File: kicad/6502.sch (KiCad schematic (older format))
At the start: 8 parts

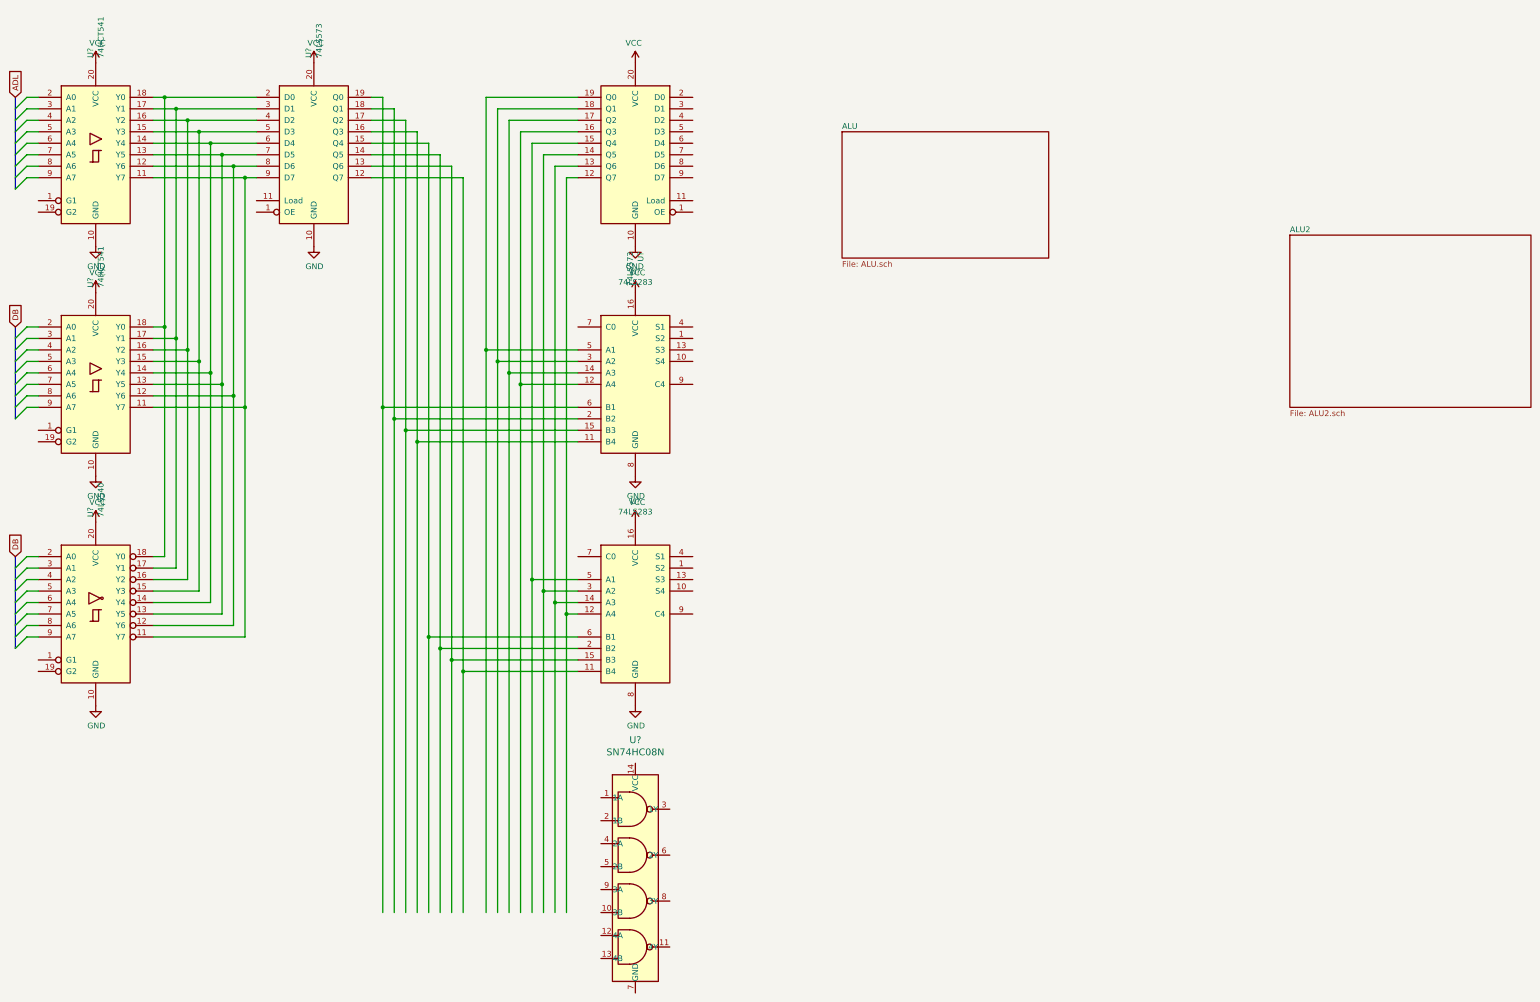
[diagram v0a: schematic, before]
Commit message: add ALU schematic
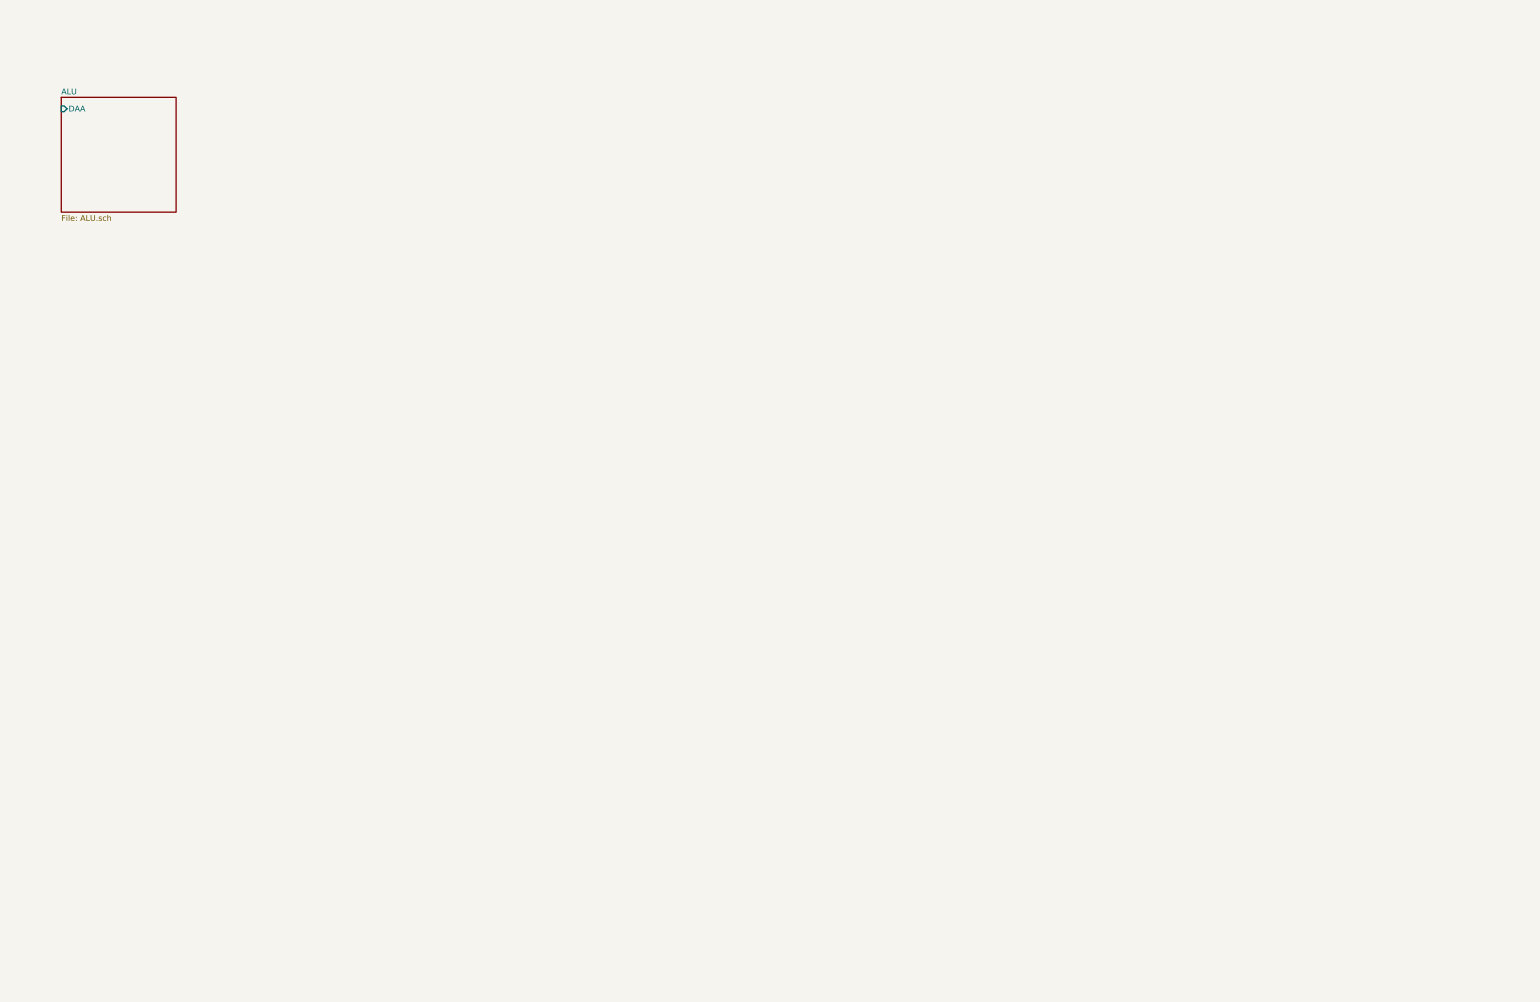
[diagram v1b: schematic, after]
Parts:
- removed U? (x2): 74LS573, symbol 74xx:74LS573
- removed U? (x2): 74HCT541, symbol 74xx:74HCT541
- removed U?: 74LS540, symbol 74xx:74LS540
- removed U? (x2): 74LS283, symbol 74xx:74LS283
- removed U?: SN74HC08N, digikey-footprints:DIP-14_W3mm, symbol dk_Logic-Gates-and-Inverters:SN74HC08N
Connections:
- net labels removed: ADL, DB, GND, VCC
- wire segments 136 -> 0

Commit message: ALU progress
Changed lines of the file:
@@
 F1 "ALU.sch" 50
 F2 "DAA" I L 1000 1100 50
+F3 "HC" I L 1000 1200 50
+F4 "1-ADDC" I L 1000 1300 50
+F5 "ACR" O R 2000 1100 50
+F6 "ADD-SB06" I L 1000 1500 50
+F7 "ADD-ADL" I L 1000 1400 50
 $EndSheet
 $EndSCHEMATC
